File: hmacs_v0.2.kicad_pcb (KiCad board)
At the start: 2 copper layers, 70 x 115 mm, 23 parts, among them J1 EXT_CONNECTOR, J2 MODULE_CONN_2, J3 SENSE_PIN_CONNECTOR, J4 MODULE_CONN_1, J5 AC_INPUT, J6 RFID_HEADER, J7 RELAY_CONNECTOR, J8 SSR_CONNECTOR, Q1 RELAY_SIG_PNP_EBC

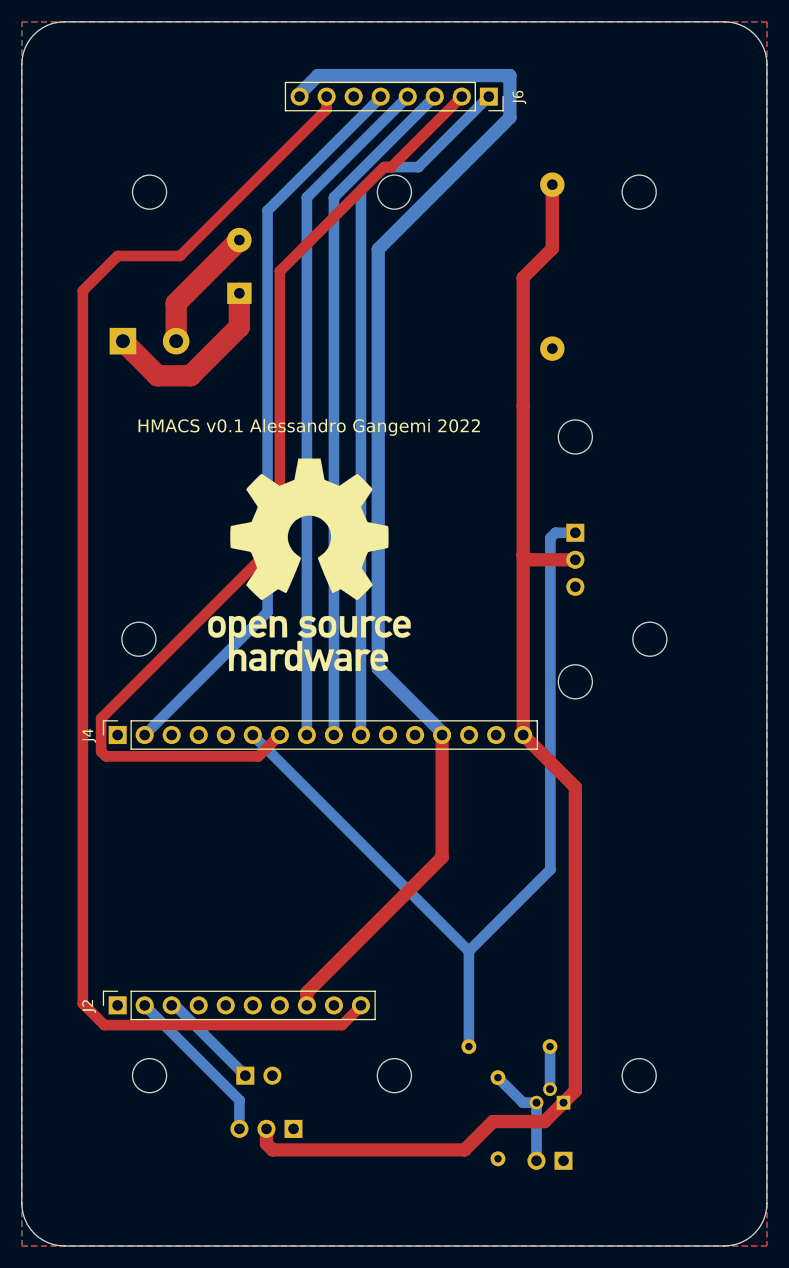
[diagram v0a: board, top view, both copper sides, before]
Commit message: Run DRC and push some things around
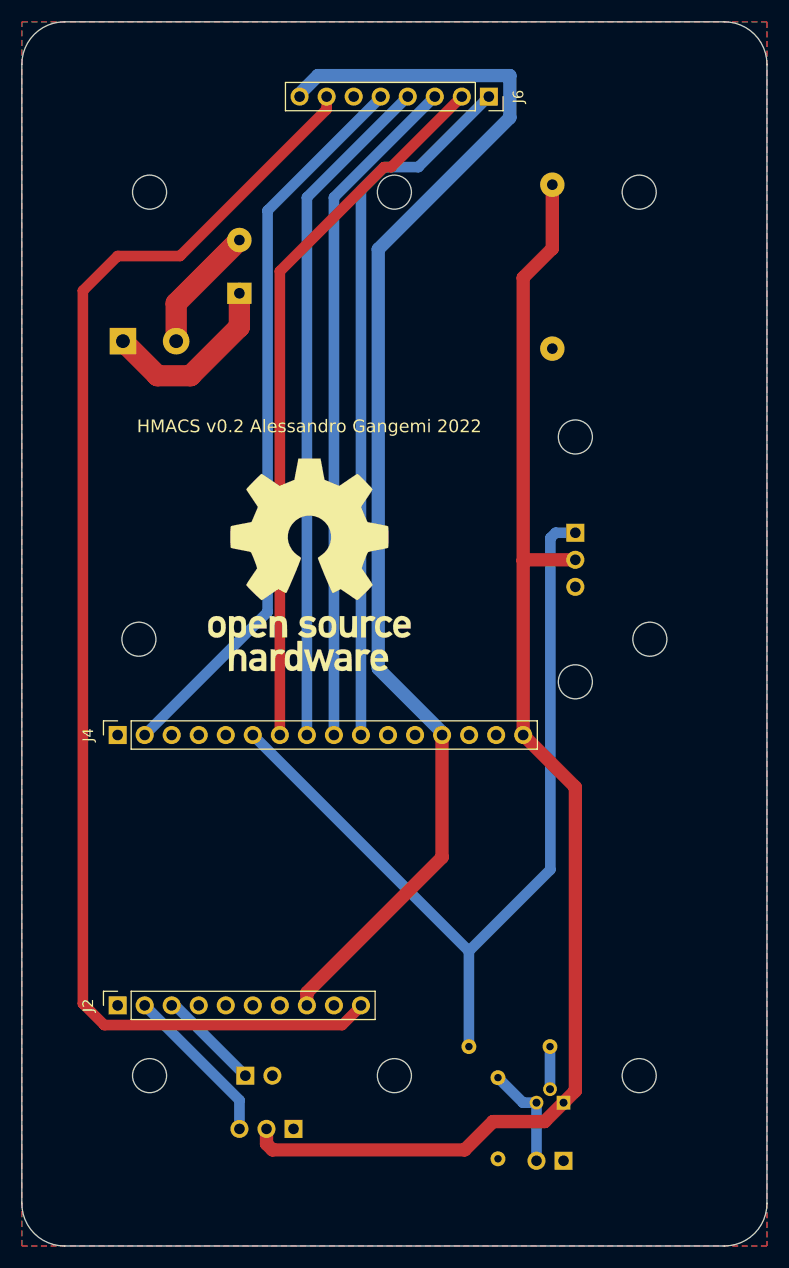
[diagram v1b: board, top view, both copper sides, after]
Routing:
- net SCK: track 93.8 -> 67.5 mm
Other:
- board text added: "CARD_PRESENT"
- board text added: "HMACS v0.2 Alessandro Gangemi 2022"
- board text removed: "EXT"
- board text removed: "HMACS v0.1 Alessandro Gangemi 2022"
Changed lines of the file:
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@@
+  )
+  (footprint "MountingHole:MountingHole_3.2mm_M3" (layer "F.Cu")
+    (at 102 97)
+    (descr "Mounting Hole 3.2mm, no annular, M3")
+    (tags "mounting hole 3.2mm no annular m3")
+    (attr exclude_from_pos_files exclude_from_bom)
+    (fp_text reference "REF**" (at 0 -4.2) (layer "F.SilkS") hide
+      (effects (font (size 1 1) (thickness 0.15)))
+    )
+    (fp_text value "MountingHole_3.2mm_M3" (at 0 4.2) (layer "F.Fab")
+      (effects (font (size 1 1) (thickness 0.15)))
+    )
+    (fp_text user "${REFERENCE}" (at 0 0) (layer "F.Fab")
+      (effects (font (size 1 1) (thickness 0.15)))
+    )
+    (fp_circle (center 0 0) (end 3.2 0) (layer "Cmts.User") (width 0.15) (fill none))
+    (fp_circle (center 0 0) (end 3.45 0) (layer "F.CrtYd") (width 0.05) (fill none))
+    (pad "" np_thru_hole circle (at 0 0) (size 3.2 3.2) (drill 3.2) (layers *.Cu *.Mask))
   )
   (footprint "MountingHole:MountingHole_3.2mm_M3" (layer "F.Cu")
@@
   )
   (footprint "MountingHole:MountingHole_3.2mm_M3" (layer "F.Cu")
-    (at 102 97)
-    (descr "Mounting Hole 3.2mm, no annular, M3")
-    (tags "mounting hole 3.2mm no annular m3")
-    (attr exclude_from_pos_files exclude_from_bom)
-    (fp_text reference "REF**" (at 0 -4.2) (layer "F.SilkS") hide
-      (effects (font (size 1 1) (thickness 0.15)))
-    )
-    (fp_text value "MountingHole_3.2mm_M3" (at 0 4.2) (layer "F.Fab")
-      (effects (font (size 1 1) (thickness 0.15)))
-    )
-    (fp_text user "${REFERENCE}" (at 0 0) (layer "F.Fab")
-      (effects (font (size 1 1) (thickness 0.15)))
-    )
-    (fp_circle (center 0 0) (end 3.2 0) (layer "Cmts.User") (width 0.15) (fill none))
-    (fp_circle (center 0 0) (end 3.45 0) (layer "F.CrtYd") (width 0.05) (fill none))
-    (pad "" np_thru_hole circle (at 0 0) (size 3.2 3.2) (drill 3.2) (layers *.Cu *.Mask))
-    (pad "" np_thru_hole circle (at 0 0) (size 3.2 3.2) (drill 3.2) (layers *.Cu *.Mask))
-  )
-  (footprint "MountingHole:MountingHole_3.2mm_M3" (layer "F.Cu")
     (at 102 74)
     (descr "Mounting Hole 3.2mm, no annular, M3")
@@
     (fp_circle (center 0 0) (end 3.2 0) (layer "Cmts.User") (width 0.15) (fill none))
     (fp_circle (center 0 0) (end 3.45 0) (layer "F.CrtYd") (width 0.05) (fill none))
-    (pad "" np_thru_hole circle (at 0 0) (size 3.2 3.2) (drill 3.2) (layers *.Cu *.Mask))
     (pad "" np_thru_hole circle (at 0 0) (size 3.2 3.2) (drill 3.2) (layers *.Cu *.Mask))
   )
@@
     (effects (font (size 1 1) (thickness 0.15)) (justify mirror))
   )
-  (gr_text "EXT" (at 78.8 139) (layer "B.SilkS")
+  (gr_text "CARD_PRESENT" (at 83.25 139) (layer "B.SilkS")
     (effects (font (size 1 1) (thickness 0.15)) (justify mirror))
   )
@@
     (effects (font (size 1 1) (thickness 0.15)) (justify mirror))
   )
-  (gr_text "HMACS v0.1 Alessandro Gangemi 2022" (at 77 73) (layer "F.SilkS")
+  (gr_text "HMACS v0.2 Alessandro Gangemi 2022" (at 77 73) (layer "F.SilkS")
     (effects (font (size 1.2 1.2) (thickness 0.25)))
   )
@@
   (segment (start 83.48452 56.364502) (end 95.849511 43.999511) (width 1.25) (layer "B.Cu") (net 1))
   (segment (start 95.849511 43.999511) (end 95.849511 40.050489) (width 1.25) (layer "B.Cu") (net 1))
-  (segment (start 89.48 102.252381) (end 89.48 102) (width 1.25) (layer "B.Cu") (net 1))
   (segment (start 77.81713 40.050489) (end 76.095 41.772619) (width 1.25) (layer "B.Cu") (net 1))
   (segment (start 70.445 136.305) (end 61.54 127.4) (width 1) (layer "B.Cu") (net 3))
@@
   (segment (start 100.15 83) (end 102 83) (width 1) (layer "B.Cu") (net 14))
   (segment (start 99.650479 83.499521) (end 100.15 83) (width 1) (layer "B.Cu") (net 14))
-  (segment (start 84.709521 48.650479) (end 91.335 42.025) (width 1) (layer "F.Cu") (net 15))
-  (segment (start 74.24 58.437274) (end 74.24 83.660978) (width 1) (layer "F.Cu") (net 15))
-  (segment (start 74.24 83.660978) (end 57.450489 100.450489) (width 1) (layer "F.Cu") (net 15))
-  (segment (start 57.450489 103.549511) (end 57.900978 104) (width 1) (layer "F.Cu") (net 15))
-  (segment (start 74.24 58.437274) (end 84.026795 48.650479) (width 1) (layer "F.Cu") (net 15))
-  (segment (start 84.026795 48.650479) (end 84.709521 48.650479) (width 1) (layer "F.Cu") (net 15))
-  (segment (start 57.900978 104) (end 72.24 104) (width 1) (layer "F.Cu") (net 15))
-  (segment (start 57.450489 100.450489) (end 57.450489 103.549511) (width 1) (layer "F.Cu") (net 15))
-  (segment (start 72.24 104) (end 74.24 102) (width 1) (layer "F.Cu") (net 15))
+  (segment (start 74.24 58.437274) (end 74.24 102) (width 1) (layer "F.Cu") (net 15))
+  (segment (start 84.709521 48.650479) (end 84.026795 48.650479) (width 1) (layer "F.Cu") (net 15))
+  (segment (start 84.026795 48.650479) (end 74.24 58.437274) (width 1) (layer "F.Cu") (net 15))
+  (segment (start 91.335 42.025) (end 84.709521 48.650479) (width 1) (layer "F.Cu") (net 15))
   (segment (start 76.78 102) (end 76.78 51.5) (width 1) (layer "B.Cu") (net 16))
   (segment (start 76.78 51.5) (end 86.255 42.025) (width 1) (layer "B.Cu") (net 16))
@@
   (segment (start 84.026795 48.650479) (end 87.249521 48.650479) (width 1) (layer "B.Cu") (net 18))
   (segment (start 87.249521 48.650479) (end 93.875 42.025) (width 1) (layer "B.Cu") (net 18))
-  (segment (start 97.1 85.1) (end 97.1 71.1) (width 1.25) (layer "F.Cu") (net 21))
   (segment (start 72.985 139) (end 72.985 140.409022) (width 1.25) (layer "F.Cu") (net 21))
+  (segment (start 97.16 85.54) (end 97.1 85.6) (width 1.25) (layer "F.Cu") (net 21))
   (segment (start 72.985 140.409022) (end 73.550489 140.974511) (width 1.25) (layer "F.Cu") (net 21))
   (segment (start 73.550489 140.974511) (end 91.600978 140.974511) (width 1.25) (layer "F.Cu") (net 21))
-  (segment (start 97.54 85.54) (end 97.1 85.1) (width 1.25) (layer "F.Cu") (net 21))
-  (segment (start 97.1 102) (end 97.1 85.1) (width 1.25) (layer "F.Cu") (net 21))
   (segment (start 99.8375 56.3) (end 99.8375 50.3) (width 1.25) (layer "F.Cu") (net 21))
+  (segment (start 97.1 85.6) (end 97.1 59.0375) (width 1.25) (layer "F.Cu") (net 21))
   (segment (start 94.260978 138.314511) (end 99.115489 138.314511) (width 1.25) (layer "F.Cu") (net 21))
   (segment (start 97.1 102) (end 102 106.9) (width 1.25) (layer "F.Cu") (net 21))
   (segment (start 99.115489 138.314511) (end 100.89 136.54) (width 1.25) (layer "F.Cu") (net 21))
+  (segment (start 97.1 102) (end 97.1 85.6) (width 1.25) (layer "F.Cu") (net 21))
   (segment (start 91.600978 140.974511) (end 94.260978 138.314511) (width 1.25) (layer "F.Cu") (net 21))
-  (segment (start 97.1 71.1) (end 97.1 59.0375) (width 1.25) (layer "F.Cu") (net 21))
-  (segment (start 102 85.54) (end 97.54 85.54) (width 1.25) (layer "F.Cu") (net 21))
+  (segment (start 102 85.54) (end 97.16 85.54) (width 1.25) (layer "F.Cu") (net 21))
   (segment (start 102 106.9) (end 102 135.43) (width 1.25) (layer "F.Cu") (net 21))
   (segment (start 97.1 59.0375) (end 99.8375 56.3) (width 1.25) (layer "F.Cu") (net 21))

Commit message: Final changes before first manufacturing run
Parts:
- J5: footprint TerminalBlock_RND:TerminalBlock_RND_205-00001_1x02_P5.00mm_Horizontal -> kf301-2p:HANDSON_KF301-2P
- moved J5 2.75 mm to (62.2, 65.0)
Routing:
- net +3V3: track 120.9 -> 116.6 mm
- net RESET: track 125.9 -> 126.4 mm
